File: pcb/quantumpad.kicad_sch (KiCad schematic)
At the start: 21 parts, among them SW2 RotaryEncoder_Switch, U17 MOUDLE-SEEEDUINO-XIAO

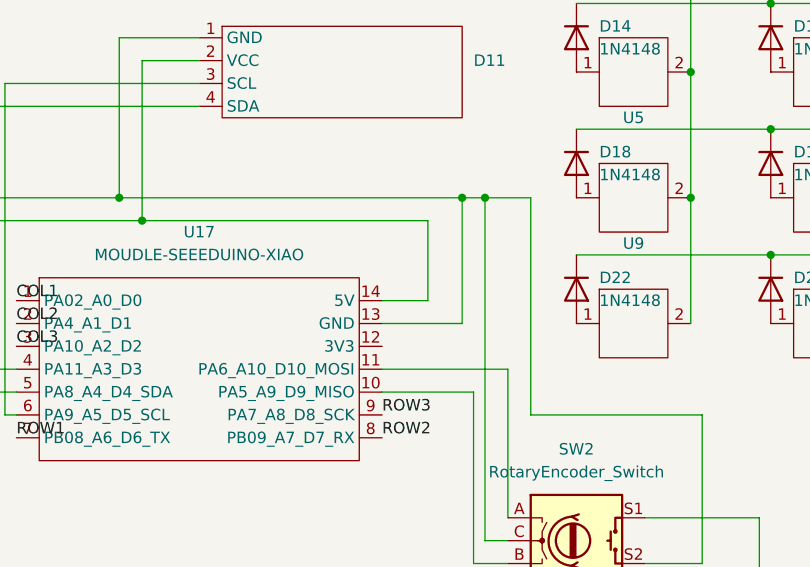
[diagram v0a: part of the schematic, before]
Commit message: Added BOM and updated images/PCB/gerber
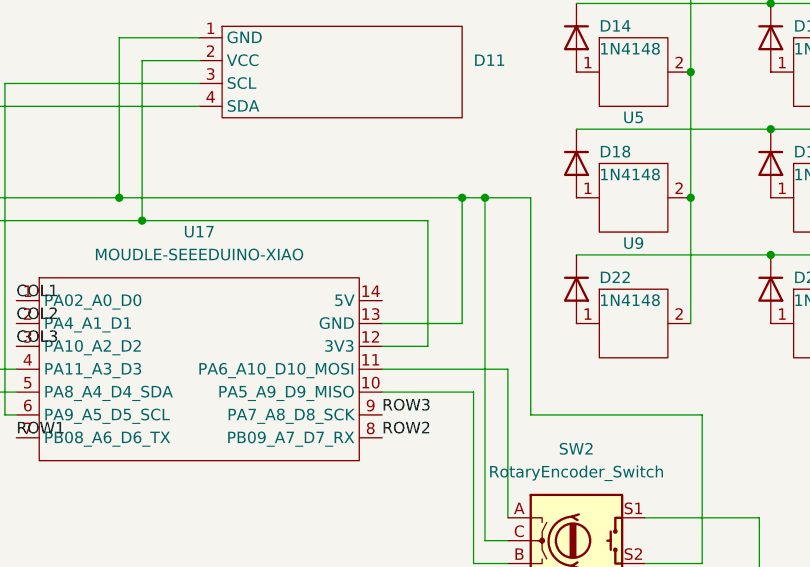
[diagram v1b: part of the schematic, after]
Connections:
- net at D11.2 (VCC): now also U17.12 (3V3); no longer U17.14 (5V)
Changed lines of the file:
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@@
 	(wire
 		(pts
-			(xy 85.09 109.22) (xy 85.09 100.33)
+			(xy 85.09 100.33) (xy 85.09 114.3)
 		)
 		(stroke
@@
 	(wire
 		(pts
+			(xy 85.09 114.3) (xy 80.01 114.3)
+		)
+		(stroke
+			(width 0)
+			(type default)
+		)
+	)
+	(wire
+		(pts
 			(xy 157.48 83.82) (xy 157.48 53.34)
 		)
@@
 		)
 		(stroke
-			(width 0)
-			(type default)
-		)
-	)
-	(wire
-		(pts
-			(xy 80.01 109.22) (xy 85.09 109.22)
-		)
-		(stroke
